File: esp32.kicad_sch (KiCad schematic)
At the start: 36 parts, among them U5 ESP32-S3R8, U6 W25Q128JVSIQ, Y1 40MHz

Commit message: routing update
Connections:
- net GROVE_PWR: no longer names the net of U5.52 (GPIO46)
- no-connect marks 5 -> 6
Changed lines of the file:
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@@
+	)
+	(no_connect
+		(at 162.56 134.62)
 	)
 	(no_connect
@@
 			(effects
 				(font
-					(size 1.27 1.27)
-				)
-				(justify left)
-				(hide yes)
-			)
-		)
-	)
-	(global_label "GROVE_PWR"
-		(shape output)
-		(at 162.56 134.62 0)
-		(fields_autoplaced yes)
-		(effects
-			(font
-				(size 1.27 1.27)
-			)
-			(justify left)
-		)
-		(property "Intersheetrefs" "${INTERSHEET_REFS}"
-			(at 176.6123 134.62 0)
-			(effects
-				(font

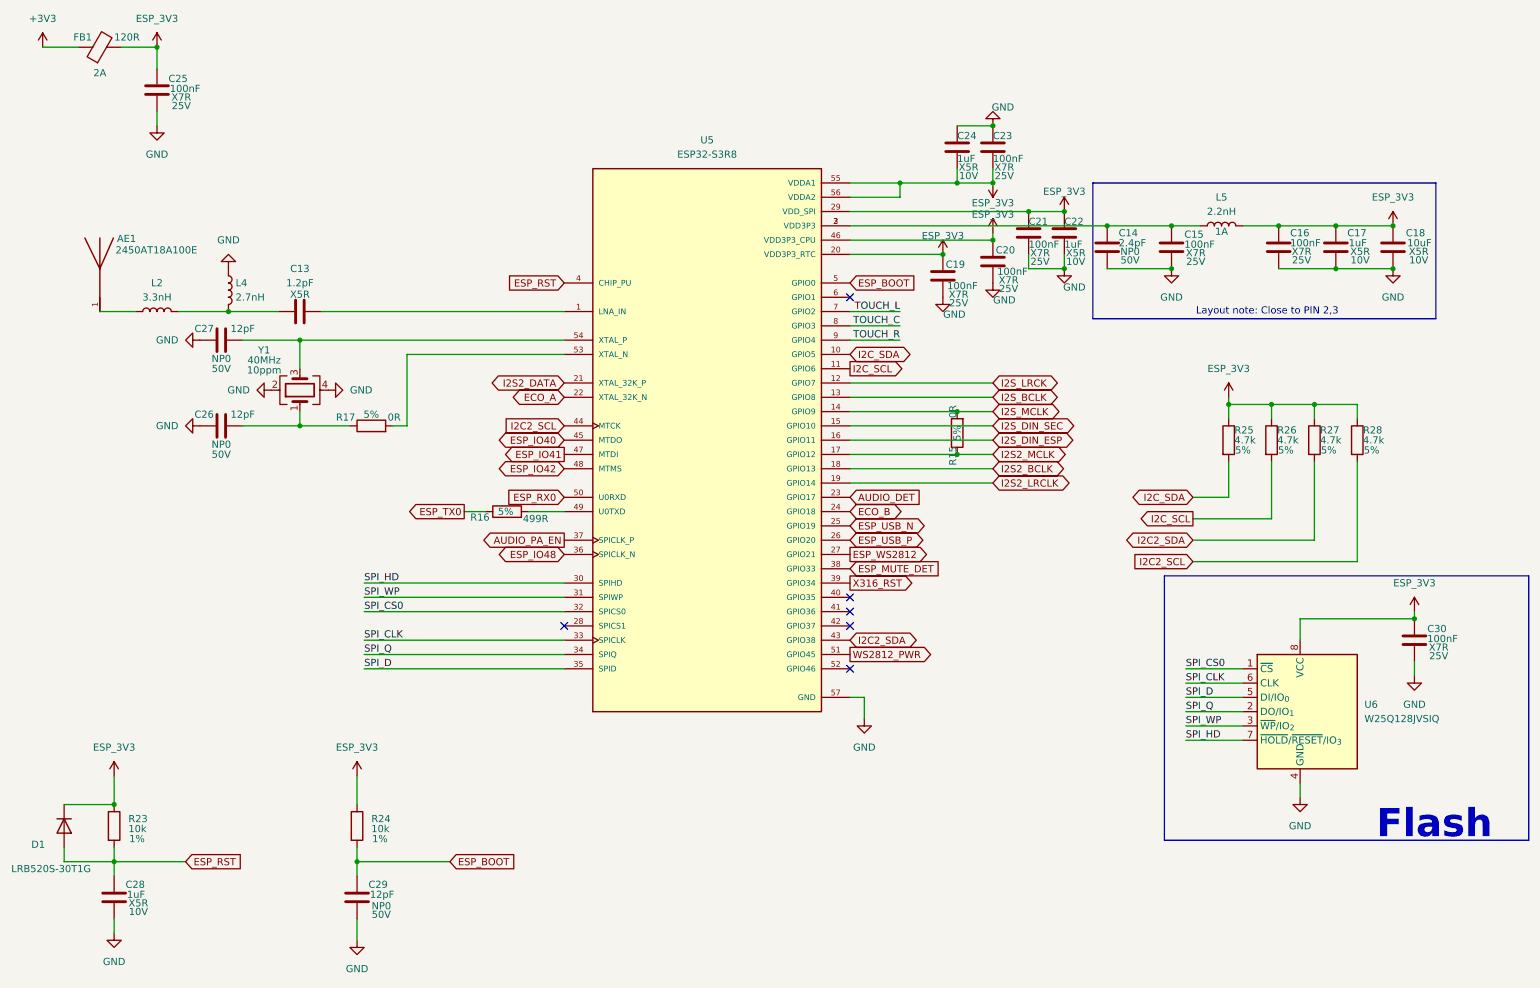
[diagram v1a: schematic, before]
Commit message: modifications for manufacturing
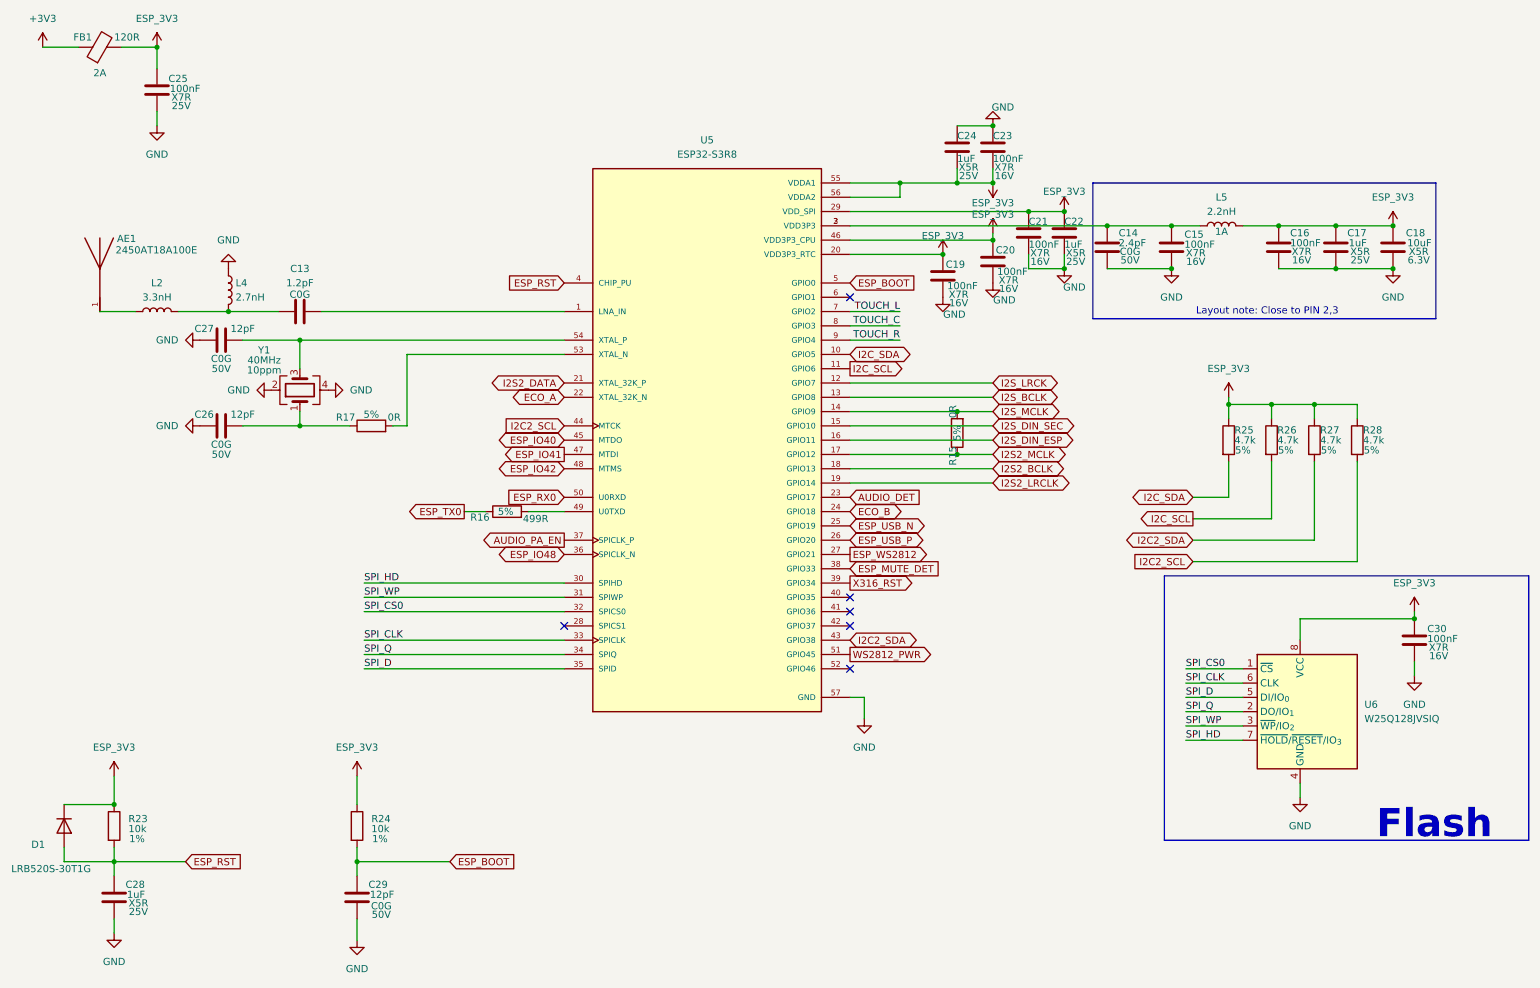
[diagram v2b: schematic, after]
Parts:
- AE1: Supplier Part (none) -> C89334
- C13: Dielectric X5R -> C0G; Supplier Part (none) -> C327292; Voltage (none) -> 10V
- C14: Dielectric NP0 -> C0G; Supplier Part (none) -> C48346
- C15, C16, C19, C20, C21, C23, C30: Supplier Part (none) -> C1525; Voltage 25V -> 16V
- C17, C22, C24, C28: Supplier Part (none) -> C52923; Voltage 10V -> 25V
- C18: Supplier Part (none) -> C15525; Voltage 10V -> 6.3V
- C25: Supplier Part (none) -> C14663
- C26, C27, C29: Dielectric NP0 -> C0G; Supplier Part (none) -> C1547
- D1: MANUFACTURER (none) -> LRC; MP (none) -> LRB520S-30T1G; Supplier Part (none) -> C83680
- FB1: MANUFACTURER (none) -> Murata Electronics; MP (none) -> BLM18PG121SN1D; Supplier Part (none) -> C14709
- L2: MANUFACTURER (none) -> Sunlord; MP (none) -> SDCL1005C3N3STDF; Supplier Part (none) -> C27124
- L4: MANUFACTURER (none) -> TDK; MP (none) -> MHQ1005P2N7BT000; Supplier Part (none) -> C434826
- L5: MANUFACTURER (none) -> Murata Electronics; MP (none) -> LQG15HS2N2B02D; Supplier Part (none) -> C162540
- R15, R17: Supplier Part (none) -> C17168
- R16: Supplier Part (none) -> C137970
- R23, R24: Supplier Part (none) -> C25744
- R25, R26, R27, R28: Supplier Part (none) -> C25900
- U5: MANUFACTURER (none) -> Espressif Systems; Supplier Part (none) -> C2913194
- U6: MANUFACTURER (none) -> Winbond Elec; MP (none) -> W25Q128JVSIQ; Supplier Part (none) -> C97521
- Y1: MANUFACTURER (none) -> YXC Crystal Oscillators; MP (none) -> X322540MPB4SI; Manufacturer (none) -> YXC Crystal Oscillators; Package (none) -> SMD3225-4P; Supplier Part (none) -> C9010

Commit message: modifications for manufacturing
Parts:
- AE1: Manufacturer (none) -> JOHANSON DESIGN; Manufacturer Part (none) -> 2450AT18A100E
- D1: Manufacturer (none) -> LRC; Manufacturer Part (none) -> LRB520S-30T1G
- FB1: Manufacturer Part (none) -> BLM18PG121SN1D
- L2: Manufacturer (none) -> Sunlord; Manufacturer Part (none) -> SDCL1005C3N3STDF
- L4: Manufacturer (none) -> TDK; Manufacturer Part (none) -> MHQ1005P2N7BT000
- L5: Manufacturer (none) -> Murata Electronics; Manufacturer Part (none) -> LQG15HS2N2B02D
- U5: Manufacturer (none) -> Espressif Systems; Manufacturer Part (none) -> ESP32-S3R8
- U6: Manufacturer (none) -> Winbond Elec; Manufacturer Part (none) -> W25Q128JVSIQ
- Y1: Manufacturer Part (none) -> X322540MPB4SI
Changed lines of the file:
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@@
 			)
 		)
+		(property "Manufacturer" "Sunlord"
+			(at 39.37 71.12 90)
+			(effects
+				(font
+					(size 1.27 1.27)
+				)
+				(hide yes)
+			)
+		)
+		(property "Manufacturer Part" "SDCL1005C3N3STDF"
+			(at 39.37 71.12 90)
+			(effects
+				(font
+					(size 1.27 1.27)
+				)
+				(hide yes)
+			)
+		)
 		(pin "2"
 		)
@@
 			)
 		)
+		(property "Manufacturer" "TDK"
+			(at 52.07 67.31 0)
+			(effects
+				(font
+					(size 1.27 1.27)
+				)
+				(hide yes)
+			)
+		)
+		(property "Manufacturer Part" "MHQ1005P2N7BT000"
+			(at 52.07 67.31 0)
+			(effects
+				(font
+					(size 1.27 1.27)
+				)
+				(hide yes)
+			)
+		)
 		(pin "2"
 		)
@@
 			)
 		)
+		(property "Manufacturer" "LRC"
+			(at 22.86 162.56 90)
+			(effects
+				(font
+					(size 1.27 1.27)
+				)
+				(hide yes)
+			)
+		)
+		(property "Manufacturer Part" "LRB520S-30T1G"
+			(at 22.86 162.56 90)
+			(effects
+				(font
+					(size 1.27 1.27)
+				)
+				(hide yes)
+			)
+		)
 		(pin "1"
 		)
@@
 			)
 		)
+		(property "Manufacturer" "Espressif Systems"
+			(at 137.16 93.98 0)
+			(effects
+				(font
+					(size 1.27 1.27)
+				)
+				(hide yes)
+			)
+		)
+		(property "Manufacturer Part" "ESP32-S3R8"
+			(at 137.16 93.98 0)
+			(effects
+				(font
+					(size 1.27 1.27)
+				)
+				(hide yes)
+			)
+		)
 		(pin "35"
 		)
@@
 			)
 		)
+		(property "Manufacturer" "Winbond Elec"
+			(at 242.57 142.24 0)
+			(effects
+				(font
+					(size 1.27 1.27)
+				)
+				(hide yes)
+			)
+		)
+		(property "Manufacturer Part" "W25Q128JVSIQ"
+			(at 242.57 142.24 0)
+			(effects
+				(font
+					(size 1.27 1.27)
+				)
+				(hide yes)
+			)
+		)
 		(pin "6"
 		)
@@
 			)
 		)
+		(property "Manufacturer" "JOHANSON DESIGN"
+			(at 29.21 66.04 0)
+			(effects
+				(font
+					(size 1.27 1.27)
+				)
+				(hide yes)
+			)
+		)
+		(property "Manufacturer Part" "2450AT18A100E"
+			(at 29.21 66.04 0)
+			(effects
+				(font
+					(size 1.27 1.27)
+				)
+				(hide yes)
+			)
+		)
 		(pin "1"
 		)
@@
 			)
 		)
+		(property "Manufacturer" "Murata Electronics"
+			(at 228.6 55.88 90)
+			(effects
+				(font
+					(size 1.27 1.27)
+				)
+				(hide yes)
+			)
+		)
+		(property "Manufacturer Part" "LQG15HS2N2B02D"
+			(at 228.6 55.88 90)
+			(effects
+				(font
+					(size 1.27 1.27)
+				)
+				(hide yes)
+			)
+		)
 		(pin "2"
 		)
@@
 			)
 		)
+		(property "Manufacturer Part" "BLM18PG121SN1D"
+			(at 29.21 24.13 90)
+			(effects
+				(font
+					(size 1.27 1.27)
+				)
+				(hide yes)
+			)
+		)
 		(pin "1"
 		)
@@
 			(at 64.77 85.09 90)
 			(effects
+				(font
+					(size 1.27 1.27)
+				)
+				(hide yes)
+			)
+		)
+		(property "Manufacturer Part" "X322540MPB4SI"
+			(at 64.77 85.09 90)
+			(effects

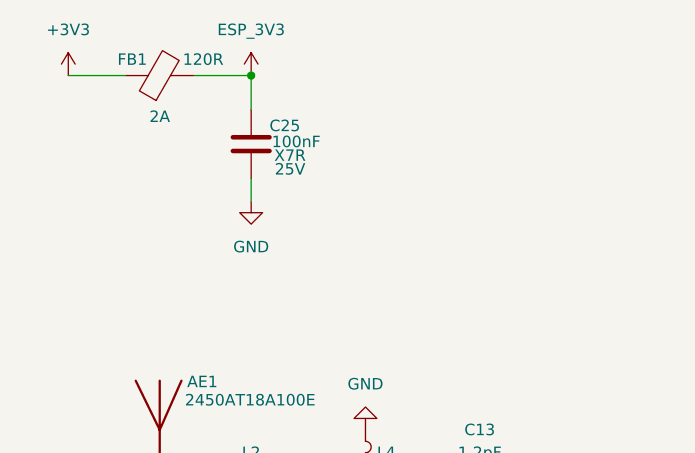
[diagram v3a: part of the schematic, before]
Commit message: modifications for manufacturing
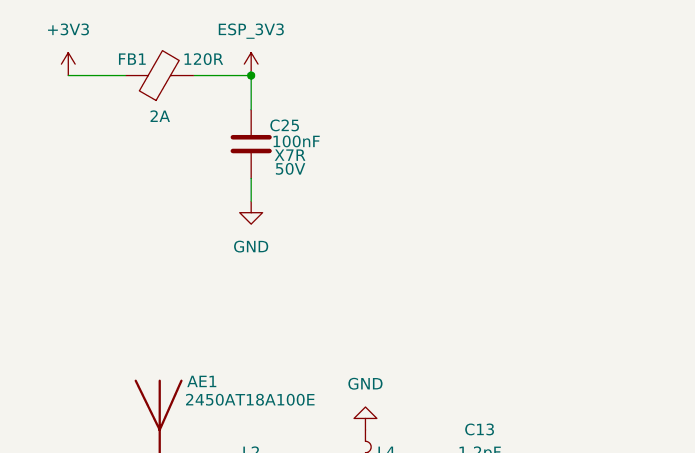
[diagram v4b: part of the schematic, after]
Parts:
- C13: Manufacturer (none) -> YAGEO; Manufacturer Part (none) -> CC0402BRNPO9BN1R2
- C14: Manufacturer (none) -> FH (Guangdong Fenghua Advanced Tech); Manufacturer Part (none) -> 0402CG2R4C500NT
- C15, C16, C19, C20, C21, C23, C30: Manufacturer (none) -> Samsung Electro-Mechanics; Manufacturer Part (none) -> CL05B104KO5NNNC
- C17, C22, C24, C28: Manufacturer (none) -> Samsung Electro-Mechanics; Manufacturer Part (none) -> CL05A105KA5NQNC
- C18: Manufacturer (none) -> Samsung Electro-Mechanics; Manufacturer Part (none) -> CL05A106MQ5NUNC
- C25: Manufacturer (none) -> YAGEO; Manufacturer Part (none) -> CC0603KRX7R9BB104; Voltage 25V -> 50V
- C26, C27, C29: Manufacturer (none) -> FH (Guangdong Fenghua Advanced Tech); Manufacturer Part (none) -> 0402CG120J500NT
- R15, R17: Manufacturer (none) -> UNI-ROYAL(Uniroyal Elec); Manufacturer Part (none) -> 0402WGF0000TCE
- R16: Manufacturer (none) -> YAGEO; Manufacturer Part (none) -> RC0402FR-07499RL
- R23, R24: Manufacturer (none) -> UNI-ROYAL(Uniroyal Elec); Manufacturer Part (none) -> 0402WGF1002TCE
- R25, R26, R27, R28: Manufacturer (none) -> UNI-ROYAL(Uniroyal Elec); Manufacturer Part (none) -> 0402WGF4701TCE

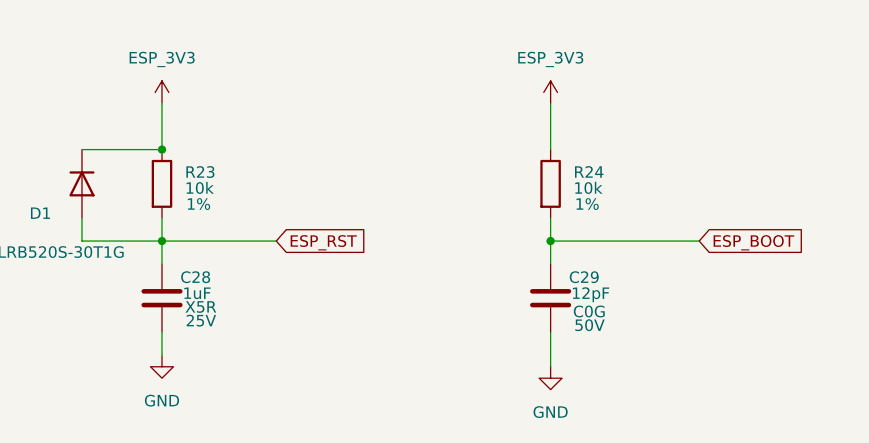
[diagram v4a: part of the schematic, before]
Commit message: modifications for manufacturing
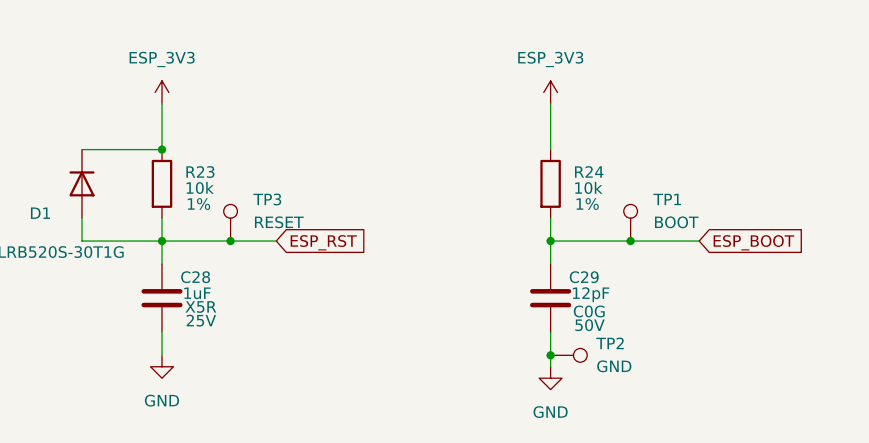
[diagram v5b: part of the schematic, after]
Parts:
- added TP1: BOOT, TestPoint:TestPoint_Pad_D1.0mm, symbol Connector:TestPoint
- added TP2: GND, TestPoint:TestPoint_Pad_D1.0mm, symbol Connector:TestPoint
- added TP3: RESET, TestPoint:TestPoint_Pad_D1.0mm, symbol Connector:TestPoint
- AE1: LCSC Part # (none) -> C89334
- C13: LCSC Part # (none) -> C327292
- C14: LCSC Part # (none) -> C48346
- C15, C16, C19, C20, C21, C23, C30: LCSC Part # (none) -> C1525
- C17, C22, C24, C28: LCSC Part # (none) -> C52923
- C18: LCSC Part # (none) -> C15525
- C25: LCSC Part # (none) -> C14663
- C26, C27, C29: LCSC Part # (none) -> C1547
- D1: LCSC Part # (none) -> C83680
- FB1: LCSC Part # (none) -> C14709
- L2: LCSC Part # (none) -> C27124
- L4: LCSC Part # (none) -> C434826
- L5: LCSC Part # (none) -> C162540
- R15, R17: LCSC Part # (none) -> C17168
- R16: LCSC Part # (none) -> C137970
- R23, R24: LCSC Part # (none) -> C25744
- R25, R26, R27, R28: LCSC Part # (none) -> C25900
- U5: LCSC Part # (none) -> C2913194
- U6: LCSC Part # (none) -> C97521
- Y1: LCSC Part # (none) -> C9010
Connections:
- net ESP_BOOT: now also TP1.1
- net ESP_RST: now also TP3.1
- net GND: now also TP2.1

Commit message: rev2 update
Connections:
- net AUDIO_DET is gone; now on net ESP_MUTE_DET: U5.23 (GPIO17)
- net WS2812_PWR is gone; now on net X316_RST: U5.51 (GPIO45)
- net ESP_MUTE_DET: no longer U5.38 (GPIO33)
- net X316_RST: no longer U5.39 (GPIO34)
- no-connect marks 6 -> 8
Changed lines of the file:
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@@
+	)
+	(no_connect
+		(at 162.56 116.84)
 	)
 	(no_connect
 		(at 162.56 134.62)
+	)
+	(no_connect
+		(at 162.56 119.38)
 	)
 	(no_connect
@@
 		)
 	)
+	(global_label "ESP_MUTE_DET"
+		(shape input)
+		(at 162.56 104.14 0)
+		(fields_autoplaced yes)
+		(effects
+			(font
+				(size 1.27 1.27)
+			)
+			(justify left)
+		)
+		(property "Intersheetrefs" "${INTERSHEET_REFS}"
+			(at 179.394 104.14 0)
+			(effects
+				(font
+					(size 1.27 1.27)
+				)
+				(justify left)
+				(hide yes)
+			)
+		)
+	)
 	(global_label "ESP_RX0"
 		(shape input)
@@
 		)
 	)
-	(global_label "X316_RST"
-		(shape output)
-		(at 162.56 119.38 0)
-		(fields_autoplaced yes)
-		(effects
-			(font
-				(size 1.27 1.27)
-			)
-			(justify left)
-		)
-		(property "Intersheetrefs" "${INTERSHEET_REFS}"
-			(at 174.7979 119.38 0)
-			(effects
-				(font
-					(size 1.27 1.27)
-				)
-				(justify left)
-				(hide yes)
-			)
-		)
-	)
 	(global_label "I2C_SCL"
 		(shape output)
@@
 		)
 	)
-	(global_label "ESP_MUTE_DET"
-		(shape input)
-		(at 162.56 116.84 0)
-		(fields_autoplaced yes)
-		(effects
-			(font
-				(size 1.27 1.27)
-			)
-			(justify left)
-		)
-		(property "Intersheetrefs" "${INTERSHEET_REFS}"
-			(at 179.394 116.84 0)
-			(effects
-				(font
-					(size 1.27 1.27)
-				)
-				(justify left)
-				(hide yes)
-			)
-		)
-	)
 	(global_label "ECO_B"
 		(shape bidirectional)
@@
 		)
 	)
+	(global_label "X316_RST"
+		(shape output)
+		(at 162.56 132.08 0)
+		(fields_autoplaced yes)
+		(effects
+			(font
+				(size 1.27 1.27)
+			)
+			(justify left)
+		)
+		(property "Intersheetrefs" "${INTERSHEET_REFS}"
+			(at 174.7979 132.08 0)
+			(effects
+				(font
+					(size 1.27 1.27)
+				)
+				(justify left)
+				(hide yes)
+			)
+		)
+	)
 	(global_label "I2S2_LRCLK"
 		(shape bidirectional)
@@
 		)
 	)
-	(global_label "WS2812_PWR"
-		(shape output)
-		(at 162.56 132.08 0)
-		(fields_autoplaced yes)
-		(effects
-			(font
-				(size 1.27 1.27)
-			)
-			(justify left)
-		)
-		(property "Intersheetrefs" "${INTERSHEET_REFS}"
-			(at 178.0031 132.08 0)
-			(effects
-				(font
-					(size 1.27 1.27)
-				)
-				(justify left)
-				(hide yes)
-			)
-		)
-	)
 	(global_label "I2S_LRCK"
 		(shape bidirectional)
@@
 			(effects
 				(font
-					(size 1.27 1.27)
-				)
-				(justify left)
-				(hide yes)
-			)
-		)
-	)
-	(global_label "AUDIO_DET"
-		(shape input)
-		(at 162.56 104.14 0)
-		(fields_autoplaced yes)
-		(effects
-			(font
-				(size 1.27 1.27)
-			)
-			(justify left)
-		)
-		(property "Intersheetrefs" "${INTERSHEET_REFS}"
-			(at 175.5238 104.14 0)
-			(effects
-				(font

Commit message: rev2 update
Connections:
- net X316_RST renamed XU316_RST
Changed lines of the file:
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@@
-		)
-	)
-	(global_label "I2C2_SDA"
-		(shape bidirectional)
-		(at 162.56 129.54 0)
-		(fields_autoplaced yes)
-		(effects
-			(font
-				(size 1.27 1.27)
-			)
-			(justify left)
-		)
-		(property "Intersheetrefs" "${INTERSHEET_REFS}"
-			(at 175.486 129.54 0)
-			(effects
-				(font
-					(size 1.27 1.27)
-				)
-				(justify left)
-				(hide yes)
-			)
 		)
 	)
@@
 	(global_label "I2C2_SDA"
 		(shape bidirectional)
+		(at 162.56 129.54 0)
+		(fields_autoplaced yes)
+		(effects
+			(font
+				(size 1.27 1.27)
+			)
+			(justify left)
+		)
+		(property "Intersheetrefs" "${INTERSHEET_REFS}"
+			(at 175.486 129.54 0)
+			(effects
+				(font
+					(size 1.27 1.27)
+				)
+				(justify left)
+				(hide yes)
+			)
+		)
+	)
+	(global_label "I2C2_SDA"
+		(shape bidirectional)
 		(at 223.52 111.76 180)
 		(fields_autoplaced yes)
@@
 		)
 	)
-	(global_label "X316_RST"
+	(global_label "XU316_RST"
 		(shape output)
 		(at 162.56 132.08 0)
@@
 		)
 		(property "Intersheetrefs" "${INTERSHEET_REFS}"
-			(at 174.7979 132.08 0)
-			(effects
-				(font
+			(at 176.1284 132.08 0)
+			(effects
+				(font

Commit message: rev2 update
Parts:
- removed TP1: BOOT, TestPoint:TestPoint_Pad_D1.0mm, symbol Connector:TestPoint
- removed TP2: GND, TestPoint:TestPoint_Pad_D1.0mm, symbol Connector:TestPoint
- removed TP3: RESET, TestPoint:TestPoint_Pad_D1.0mm, symbol Connector:TestPoint
- added SW2: BOOT, Onju:SW-SMD_4P-L4.2-W3.2-P2.15-LS4.5, symbol Switch:SW_Push
- added SW3: Reset, Onju:SW-SMD_4P-L4.2-W3.2-P2.15-LS4.5, symbol Switch:SW_Push
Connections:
- net ESP_BOOT: now also SW2.1
- net ESP_RST: now also SW3.1
- net GND: now also SW2.2, SW3.2
